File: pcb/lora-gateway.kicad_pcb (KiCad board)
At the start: 2 copper layers, 78.3 x 25.8 mm, 18 parts, among them J1 USB_B_Micro, J2 Conn_01x06, J3 Conn_01x06, J4 Conn_Coaxial, J5 AVR-JTAG-10, J6 AVR-ISP-6, SW1 SW_Push, U1 RFM95W-868S2, U2 ATmega2560-16A, U3 LM1117-3.3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

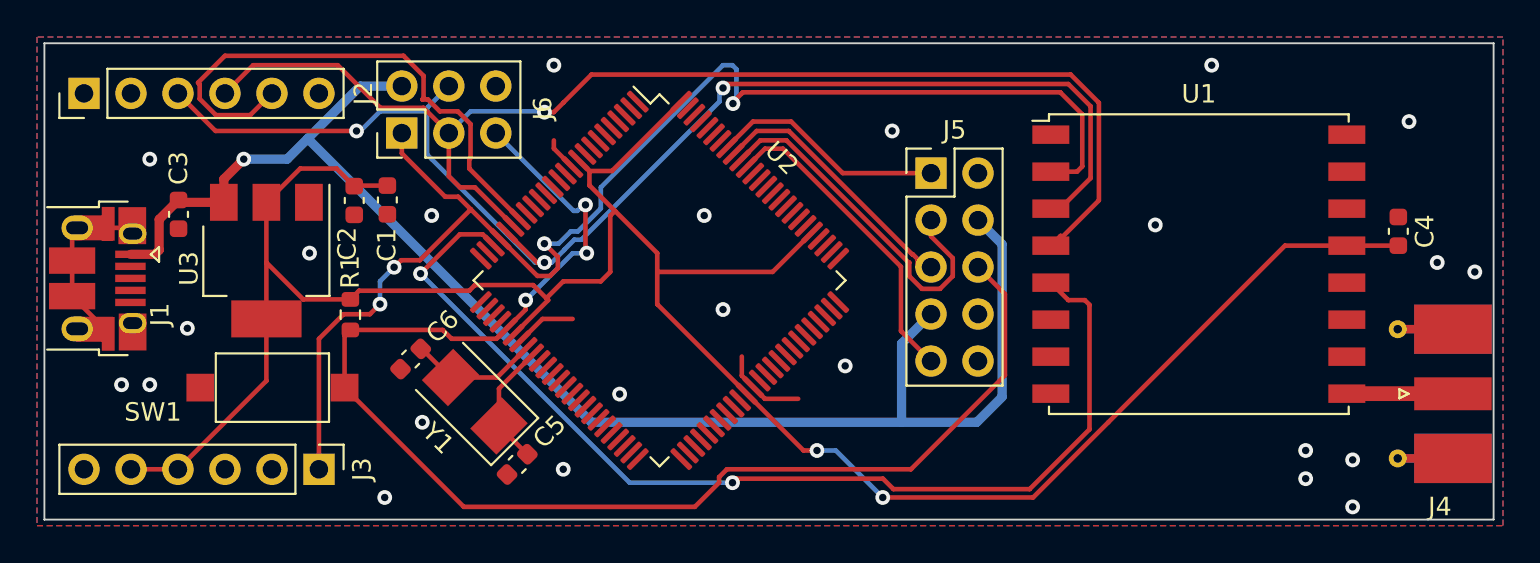
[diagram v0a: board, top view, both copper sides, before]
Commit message: add leds
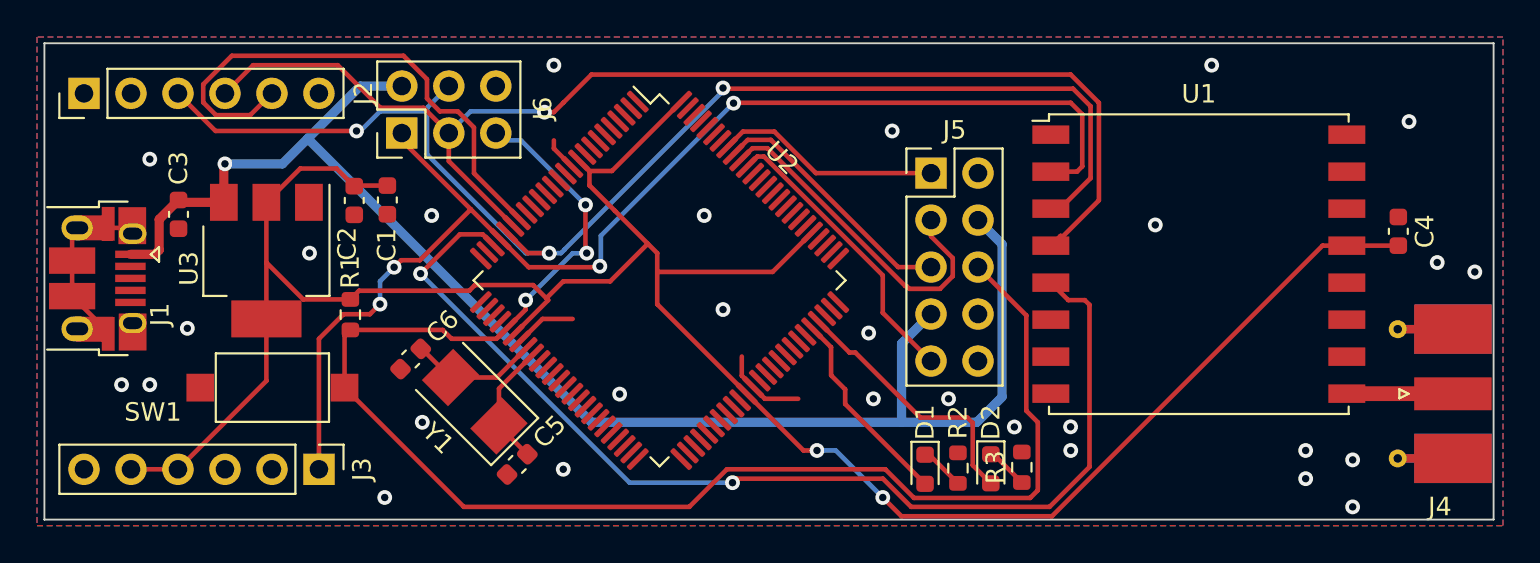
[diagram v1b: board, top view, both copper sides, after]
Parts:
- added D1: LED, LED_SMD:LED_0603_1608Metric, F.Cu at (86.1, 81.3)
- added D2: LED, LED_SMD:LED_0603_1608Metric, F.Cu at (89.7, 81.3)
- added R2: R_Small, Resistor_SMD:R_0603_1608Metric, F.Cu at (87.9, 81.2)
- added R3: R_Small, Resistor_SMD:R_0603_1608Metric, F.Cu at (91.3, 81.2)
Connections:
- U2 pad 71: unconnected-(U2-PA7-Pad71) -> LED2
- U2 pad 72: unconnected-(U2-PA6-Pad72) -> LED1
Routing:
- net LED1: track 0.00 -> 14.3 mm
- net LED2: track 0.00 -> 10.9 mm
- net RST: track 75.8 -> 82.7 mm
- net MISO: track 74.3 -> 68.4 mm
- net Net-(D1-K): track 0.00 -> 2.42 mm
- net Net-(D2-K): track 0.00 -> 2.31 mm
- net SS_LORA: track 56.9 -> 58.9 mm
- net TDI: track 17.2 -> 16.0 mm
- net TDO: track 19.5 -> 18.7 mm
- net MOSI: track 71.5 -> 70.7 mm
- net SS_ETH: track 29.7 -> 28.9 mm
- net TMS: track 14.5 -> 13.8 mm
- net GND: vias 24 -> 29
